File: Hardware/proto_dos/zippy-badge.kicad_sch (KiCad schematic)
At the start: 47 parts, among them J1 Micro_SD_Card_SPI, J2 USB-C, J3 Conn_01x08, J4 Conn_01x10, SW1 Boot Select, SW2 SW_SPDT, SW3 SKRHABE010, U1 NCP115ASN330T2G, U2 RP2040, U3 W25Q32RV, U4 GSDA213, X1 Badgelife_sao_connector_v169b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, Y1 ABM8-272-T3

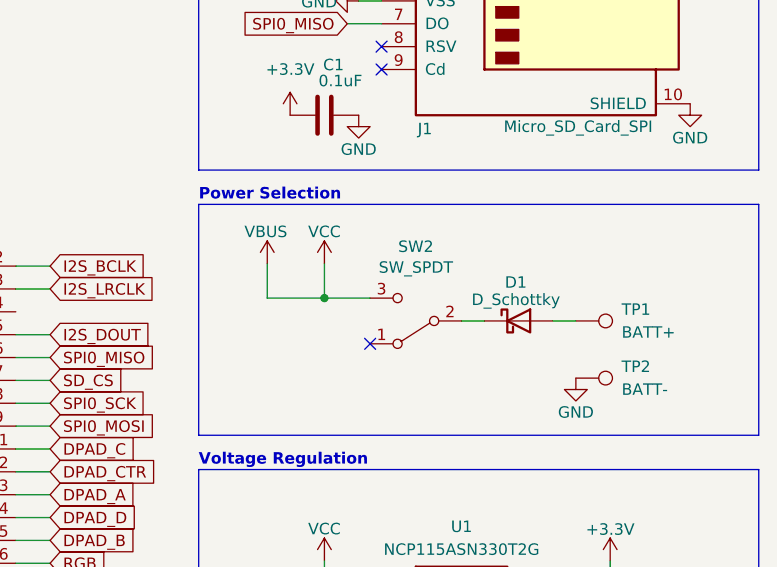
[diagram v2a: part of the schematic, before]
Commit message: Adding artwork to the back Added blocking diode for VBUS Added outputs
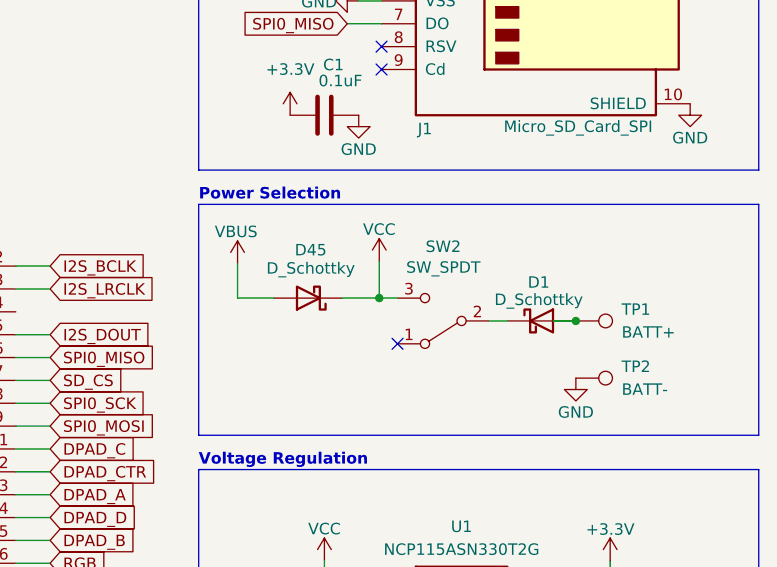
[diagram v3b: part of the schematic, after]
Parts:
- added D45: D_Schottky, Diode_SMD:D_SOD-123F, symbol Device:D_Schottky
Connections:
- net VBUS: now also D45.2 (A); no longer C9.2, SW2.3 (C), U1.1 (IN), U1.3 (EN)
- new net VCC: C9.2, D45.1 (K), SW2.3 (C), U1.1 (IN), U1.3 (EN)
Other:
- moved on the sheet: D1, SW2
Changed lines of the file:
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@@
 	)
 	(junction
+		(at 218.186 69.85)
+		(diameter 0)
+		(color 0 0 0 0)
+	)
+	(junction
 		(at 81.534 192.024)
 		(diameter 0)
@@
 	)
 	(junction
-		(at 212.09 69.85)
+		(at 212.09 101.6)
 		(diameter 0)
 		(color 0 0 0 0)
 	)
 	(junction
-		(at 212.09 101.6)
+		(at 152.4 151.13)
 		(diameter 0)
 		(color 0 0 0 0)
 	)
 	(junction
-		(at 152.4 151.13)
+		(at 243.84 101.6)
 		(diameter 0)
 		(color 0 0 0 0)
 	)
 	(junction
-		(at 243.84 101.6)
+		(at 240.03 72.39)
 		(diameter 0)
 		(color 0 0 0 0)
@@
 	)
 	(no_connect
-		(at 217.17 74.93)
+		(at 220.218 74.93)
 	)
 	(wire
@@
 	(wire
 		(pts
-			(xy 205.74 69.85) (xy 212.09 69.85)
-		)
-		(stroke
-			(width 0)
-			(type default)
-		)
-	)
-	(wire
-		(pts
 			(xy 181.61 127.254) (xy 177.8 127.254)
 		)
@@
 	(wire
 		(pts
-			(xy 227.33 72.39) (xy 229.87 72.39)
+			(xy 230.378 72.39) (xy 232.41 72.39)
 		)
 		(stroke
@@
 	(wire
 		(pts
+			(xy 214.122 69.85) (xy 218.186 69.85)
+		)
+		(stroke
+			(width 0)
+			(type default)
+		)
+	)
+	(wire
+		(pts
 			(xy 181.61 91.694) (xy 177.8 91.694)
 		)
@@
 	(wire
 		(pts
+			(xy 218.186 69.85) (xy 220.218 69.85)
+		)
+		(stroke
+			(width 0)
+			(type default)
+		)
+	)
+	(wire
+		(pts
 			(xy 26.67 127.508) (xy 25.654 127.508)
 		)
@@
 	(wire
 		(pts
-			(xy 212.09 66.04) (xy 212.09 69.85)
+			(xy 218.186 65.786) (xy 218.186 69.85)
 		)
 		(stroke
@@
 	(wire
 		(pts
-			(xy 212.09 69.85) (xy 217.17 69.85)
-		)
-		(stroke
-			(width 0)
-			(type default)
-		)
-	)
-	(wire
-		(pts
 			(xy 160.02 20.574) (xy 157.48 20.574)
 		)
@@
 	(wire
 		(pts
-			(xy 205.74 66.04) (xy 205.74 69.85)
+			(xy 202.438 66.04) (xy 202.438 69.85)
 		)
 		(stroke
@@
 	(wire
 		(pts
+			(xy 202.438 69.85) (xy 206.502 69.85)
+		)
+		(stroke
+			(width 0)
+			(type default)
+		)
+	)
+	(wire
+		(pts
 			(xy 243.84 110.49) (xy 243.84 111.76)
 		)
@@
 	)
 	(symbol
+		(lib_id "Device:D_Schottky")
+		(at 210.312 69.85 180)
+		(unit 1)
+		(exclude_from_sim no)
+		(in_bom yes)
+		(on_board yes)
+		(dnp no)
+		(property "Reference" "D45"
+			(at 210.566 64.516 0)
+			(effects
+				(font
+					(size 1.27 1.27)
+				)
+			)
+		)
+		(property "Value" "D_Schottky"
+			(at 210.566 66.548 0)
+			(effects
+				(font
+					(size 1.27 1.27)
+				)
+			)
+		)
+		(property "Footprint" "Diode_SMD:D_SOD-123F"
+			(at 210.312 69.85 0)
+			(effects
+				(font
+					(size 1.27 1.27)
+				)
+				(hide yes)
+			)
+		)
+		(property "Datasheet" "~"
+			(at 210.312 69.85 0)
+			(effects
+				(font
+					(size 1.27 1.27)
+				)
+				(hide yes)
+			)
+		)
+		(property "Description" ""
+			(at 210.312 69.85 0)
+			(effects
+				(font
+					(size 1.27 1.27)
+				)
+				(hide yes)
+			)
+		)
+		(pin "1"
+		)
+		(pin "2"
+		)
+		(instances
+			(project "zippy-badge"
+				(path "/2f5e3b6b-e0ac-4904-9222-e2ea7797e398"
+					(reference "D45")
+					(unit 1)
+				)
+			)
+		)
+	)
+	(symbol
 		(lib_id "Device:Crystal_GND24")
 		(at 32.512 90.678 90)
@@
 	(symbol
 		(lib_id "power:VCC")
-		(at 205.74 66.04 0)
+		(at 202.438 66.04 0)
 		(unit 1)
 		(exclude_from_sim no)
@@
 		(dnp no)
 		(property "Reference" "#PWR011"
-			(at 205.74 69.85 0)
+			(at 202.438 69.85 0)
 			(effects
 				(font
@@
 		)
 		(property "Value" "VBUS"
-			(at 203.2 62.484 0)
+			(at 199.898 62.484 0)
 			(effects
 				(font
@@
 		)
 		(property "Footprint" ""
-			(at 205.74 66.04 0)
+			(at 202.438 66.04 0)
 			(effects
 				(font
@@
 		)
 		(property "Datasheet" ""
-			(at 205.74 66.04 0)
+			(at 202.438 66.04 0)
 			(effects
 				(font
@@
 		)
 		(property "Description" ""
-			(at 205.74 66.04 0)
+			(at 202.438 66.04 0)
 			(effects
 				(font
@@
 	(symbol
 		(lib_id "Switch:SW_SPDT")
-		(at 222.25 72.39 180)
+		(at 225.298 72.39 180)
 		(unit 1)
 		(exclude_from_sim no)
@@
 		(dnp no)
 		(property "Reference" "SW2"
-			(at 222.25 64.135 0)
+			(at 225.298 64.135 0)
 			(effects
 				(font
@@
 		)
 		(property "Value" "SW_SPDT"
-			(at 222.25 66.4464 0)
+			(at 225.298 66.4464 0)
 			(effects
 				(font
@@
 		)
 		(property "Footprint" "lib_fp:SW_SPDT_CK-JS102011SAQN"
-			(at 222.25 72.39 0)
+			(at 225.298 72.39 0)
 			(effects
 				(font
@@
 		)
 		(property "Datasheet" ""
-			(at 222.25 72.39 0)
+			(at 225.298 72.39 0)
 			(effects
 				(font
@@
 		)
 		(property "Description" ""
-			(at 222.25 72.39 0)
+			(at 225.298 72.39 0)
 			(effects
 				(font
@@
 		(lib_name "VCC_2")
 		(lib_id "power:VCC")
-		(at 212.09 66.04 0)
+		(at 218.186 65.786 0)
 		(unit 1)
 		(exclude_from_sim no)
@@
 		(dnp no)
 		(property "Reference" "#PWR12"
-			(at 212.09 69.85 0)
+			(at 218.186 69.596 0)
 			(effects
 				(font
@@
 		)
 		(property "Value" "VCC"
-			(at 212.09 62.484 0)
+			(at 218.186 62.23 0)
 			(effects
 				(font
@@
 		)
 		(property "Footprint" ""
-			(at 212.09 66.04 0)
+			(at 218.186 65.786 0)
 			(effects
 				(font
@@
 		)
 		(property "Datasheet" ""
-			(at 212.09 66.04 0)
+			(at 218.186 65.786 0)
 			(effects
 				(font
@@
 		)
 		(property "Description" "Power symbol creates a global label with name \"VCC\""
-			(at 212.09 66.04 0)
+			(at 218.186 65.786 0)
 			(effects
 				(font
@@
 	(symbol
 		(lib_id "Device:D_Schottky")
-		(at 233.68 72.39 0)
+		(at 236.22 72.39 0)
 		(unit 1)
 		(exclude_from_sim no)
@@
 		(fields_autoplaced yes)
 		(property "Reference" "D1"
-			(at 233.3625 68.1101 0)
+			(at 235.9025 68.1101 0)
 			(effects
 				(font
@@
 		)
 		(property "Value" "D_Schottky"
-			(at 233.3625 70.0311 0)
+			(at 235.9025 70.0311 0)
 			(effects
 				(font
@@
 		)
 		(property "Footprint" "Diode_SMD:D_SOD-123F"
-			(at 233.68 72.39 0)
+			(at 236.22 72.39 0)
 			(effects
 				(font
@@
 		)
 		(property "Datasheet" "~"
-			(at 233.68 72.39 0)
+			(at 236.22 72.39 0)
 			(effects
 				(font
@@
 		)
 		(property "Description" ""
-			(at 233.68 72.39 0)
+			(at 236.22 72.39 0)
 			(effects
 				(font

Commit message: Final updates before board order
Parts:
- added TP3, TP4, TP5, TP6: ~, TestPoint:TestPoint_Pad_1.0x1.0mm, symbol Connector:TestPoint
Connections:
- net at U2.17 (GPIO14): now also TP4.1
- net at U2.18 (GPIO15): now also TP5.1
- net at U2.4 (GPIO2): now also TP3.1
- net at U2.41 (GPIO29_ADC3): now also TP6.1
- no-connect marks 4 -> 8
